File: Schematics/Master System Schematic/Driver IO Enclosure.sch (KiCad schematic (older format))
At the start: 5 parts, among them U11 CAN_Bus_Module, U12 KY-019

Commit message: Added Master Schematic Wiring
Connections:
- new net: A1.~ (~~D9), U11.~ (Serial_Clock) (x6)
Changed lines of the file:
@@
 EESchema Schematic File Version 4
+LIBS:Master System Schematic-cache
 EELAYER 30 0
 EELAYER END

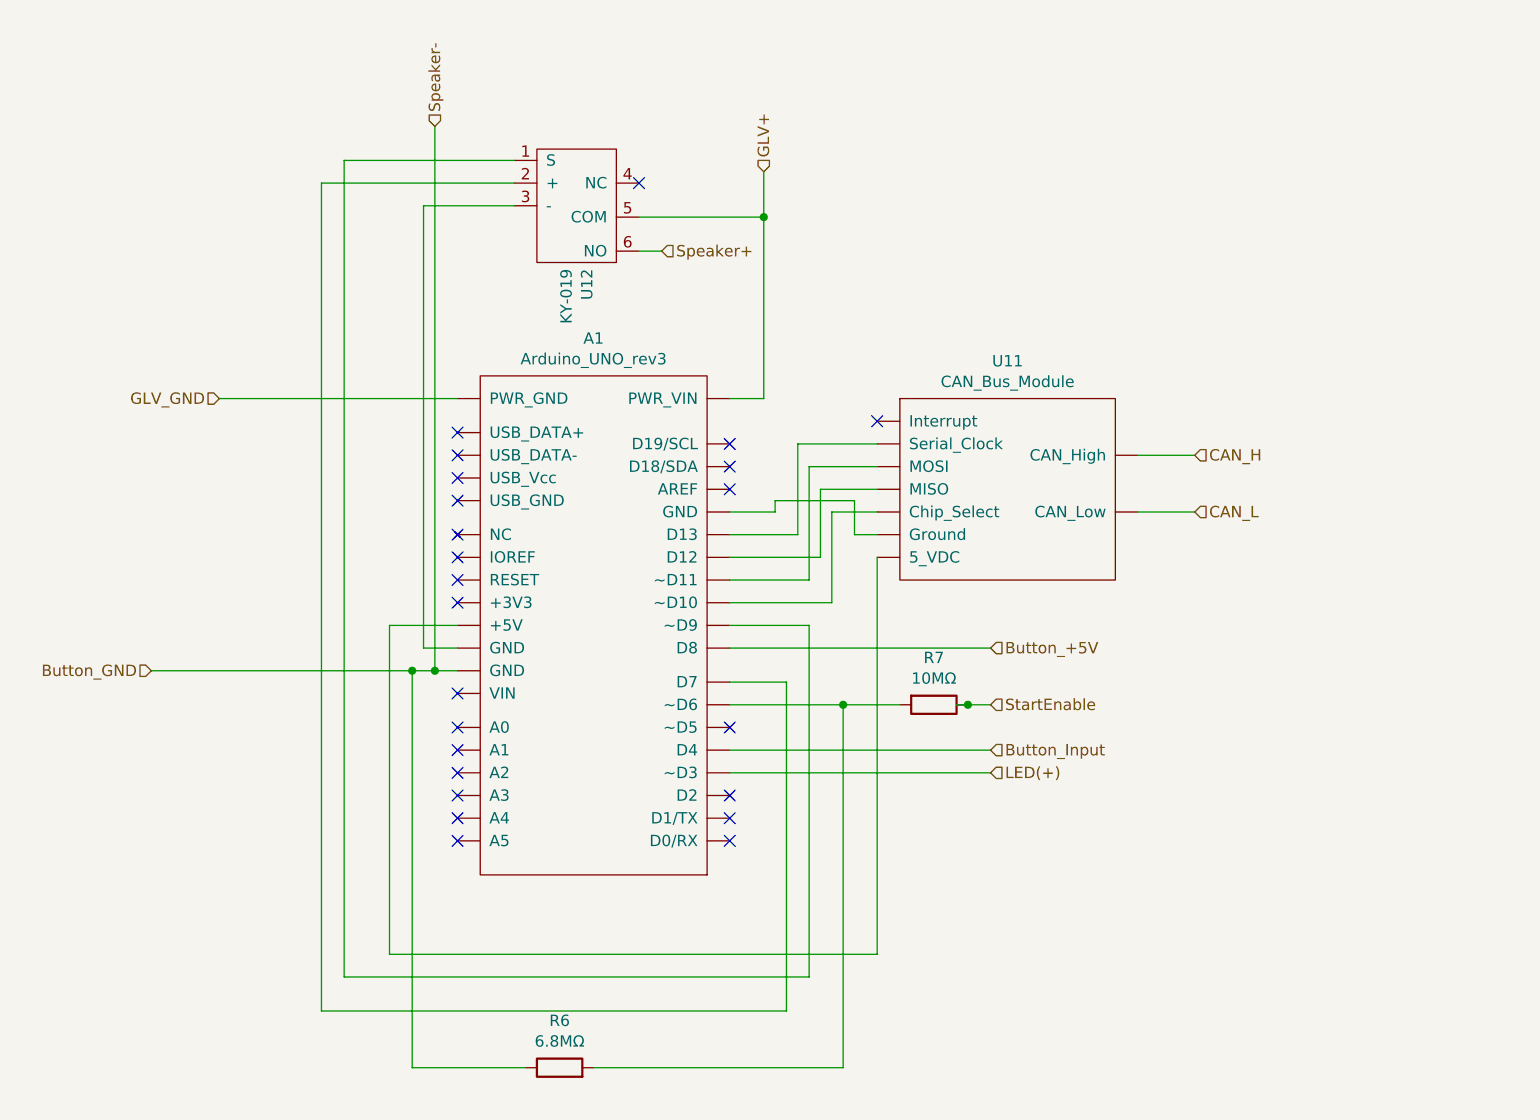
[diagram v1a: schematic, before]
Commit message: Cleaned up/Finalized Driver IO Schematic
Added a 100 ohm resistor to the 3v button to drop the 5v from the arduino to 3v. Cleaned up the messy wires.
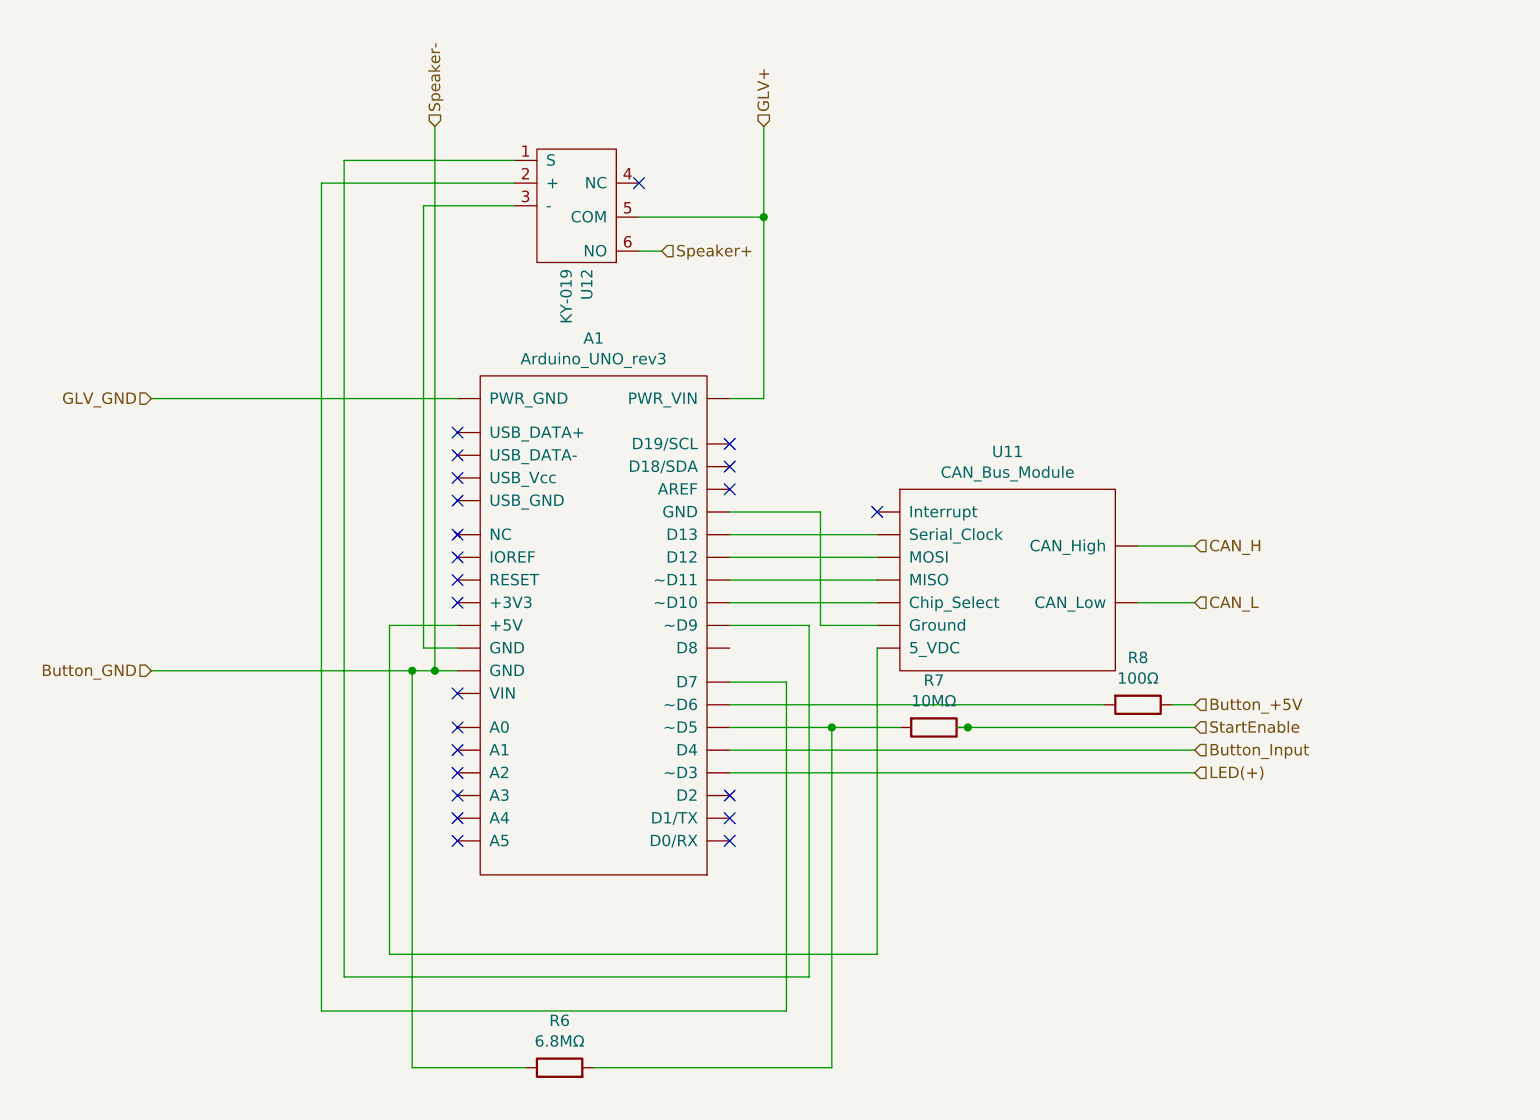
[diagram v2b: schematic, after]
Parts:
- added R8: 100Ω, symbol Device:R
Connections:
- net Button_+5V: now also R8.1; no longer A1.~ (~~D9)
- new net: A1.~ (~~D9), U11.~ (Serial_Clock) (x6)
- new net: A1.~ (~~D9), R8.2
- no-connect marks 24 -> 23
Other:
- moved on the sheet: R7, U11
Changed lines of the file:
@@
 EESchema Schematic File Version 4
-LIBS:Master System Schematic-cache
 EELAYER 30 0
 EELAYER END
@@
 $EndDescr
 $Comp
-L NER:CAN_Bus_Module U11
-U 1 1 5F847676
-P 7250 2900
-F 0 "U11" H 7275 3015 50  0000 C CNN
-F 1 "CAN_Bus_Module" H 7275 2924 50  0000 C CNN
-F 2 "" H 7250 2900 50  0001 C CNN
-F 3 "" H 7250 2900 50  0001 C CNN
-	1    7250 2900
-	1    0    0    -1
-$EndComp
-$Comp
 L NER:Arduino_UNO_rev3 A1
 U 1 1 5F848DBE
@@
 	0    1    1    0
 $EndComp
-Text HLabel 8100 3450 2    50   Input ~ 0
-CAN_L
-Wire Wire Line
-	8100 3450 7850 3450
-Text HLabel 8100 3200 2    50   Input ~ 0
-CAN_H
-Wire Wire Line
-	8100 3200 7850 3200
-Text HLabel 6200 1950 1    50   Input ~ 0
+Text HLabel 6200 1750 1    50   Input ~ 0
 GLV+
 Wire Wire Line
 	6200 2950 6050 2950
-NoConn ~ 6700 3050
-Wire Wire Line
-	6700 3150 6350 3150
-Wire Wire Line
-	6350 3150 6350 3550
-Wire Wire Line
-	6350 3550 6050 3550
-Wire Wire Line
-	6200 1950 6200 2150
 Wire Wire Line
 	6200 2150 5650 2150
@@
 	4750 1750 4750 4150
 Wire Wire Line
-	6700 3250 6400 3250
-Wire Wire Line
-	6400 3250 6400 3750
-Wire Wire Line
-	6400 3750 6050 3750
-Wire Wire Line
-	6700 3350 6450 3350
-Wire Wire Line
-	6450 3350 6450 3650
-Wire Wire Line
-	6450 3650 6050 3650
-Wire Wire Line
-	6700 3450 6500 3450
-Wire Wire Line
-	6500 3450 6500 3850
-Wire Wire Line
-	6500 3850 6050 3850
-Wire Wire Line
-	6700 3550 6600 3550
-Wire Wire Line
-	6600 3550 6600 3400
-Wire Wire Line
-	6600 3400 6250 3400
-Wire Wire Line
-	6250 3400 6250 3450
-Wire Wire Line
-	6250 3450 6050 3450
-Wire Wire Line
-	6700 3650 6700 5400
-Wire Wire Line
 	6700 5400 4550 5400
 Wire Wire Line
@@
 Wire Wire Line
 	6400 3950 6050 3950
-Text HLabel 3800 2950 0    50   Input ~ 0
+Text HLabel 3500 2950 0    50   Input ~ 0
 GLV_GND
-Wire Wire Line
-	4850 2950 3800 2950
 NoConn ~ 5650 2000
 Wire Wire Line
@@
 NoConn ~ 4850 4800
 NoConn ~ 4850 4900
-NoConn ~ 6050 4400
 NoConn ~ 6050 4700
 NoConn ~ 6050 4800
@@
 NoConn ~ 6050 3250
 NoConn ~ 6050 3350
-Wire Wire Line
-	6050 4600 7200 4600
-Text HLabel 7200 4600 2    50   Input ~ 0
+Text HLabel 8100 4600 2    50   Input ~ 0
 LED(+)
 Wire Wire Line
@@
 Text HLabel 3500 4150 0    50   Input ~ 0
 Button_GND
-Text HLabel 7200 4500 2    50   Input ~ 0
+Text HLabel 8100 4500 2    50   Input ~ 0
 Button_Input
-Wire Wire Line
-	6050 4500 7200 4500
-Text HLabel 7200 4050 2    50   Input ~ 0
+Text HLabel 8100 4300 2    50   Input ~ 0
 Button_+5V
-Wire Wire Line
-	6050 4050 7200 4050
 Text HLabel 5750 2300 2    50   Input ~ 0
 Speaker+
@@
 Wire Wire Line
 	5650 2300 5750 2300
-Text HLabel 7200 4300 2    50   Input ~ 0
-StartEnable
-$Comp
-L Device:R R7
-U 1 1 5F8BB898
-P 6950 4300
-F 0 "R7" V 6743 4300 50  0000 C CNN
-F 1 "10MΩ" V 6834 4300 50  0000 C CNN
-F 2 "" V 6880 4300 50  0001 C CNN
-F 3 "~" H 6950 4300 50  0001 C CNN
-	1    6950 4300
-	0    1    1    0
-$EndComp
-Wire Wire Line
-	7200 4300 7100 4300
-Connection ~ 7100 4300
-Wire Wire Line
-	7100 4300 7050 4300
-Wire Wire Line
-	6050 4300 6550 4300
 $Comp
 L Device:R R6
@@
 $EndComp
 Wire Wire Line
-	6550 4300 6550 5900
-Wire Wire Line
-	6550 5900 5450 5900
-Connection ~ 6550 4300
-Wire Wire Line
-	6550 4300 6800 4300
-Wire Wire Line
 	4650 5900 4650 4150
 Wire Wire Line
@@
 Wire Wire Line
 	4650 4150 4750 4150
+$Comp
+L Device:R R8
+U 1 1 5F8E0B40
+P 7850 4300
+F 0 "R8" V 7643 4300 50  0000 C CNN
+F 1 "100Ω" V 7734 4300 50  0000 C CNN
+F 2 "" V 7780 4300 50  0001 C CNN
+F 3 "~" H 7850 4300 50  0001 C CNN
+	1    7850 4300
+	0    1    1    0
+$EndComp
+Wire Wire Line
+	8000 4300 8100 4300
+NoConn ~ 6700 3450
+Wire Wire Line
+	8100 3600 7850 3600
+Text HLabel 8100 3600 2    50   Input ~ 0
+CAN_H
+Wire Wire Line
+	8100 3850 7850 3850
+Text HLabel 8100 3850 2    50   Input ~ 0
+CAN_L
+$Comp
+L NER:CAN_Bus_Module U11
+U 1 1 5F847676
+P 7250 3300
+F 0 "U11" H 7275 3415 50  0000 C CNN
+F 1 "CAN_Bus_Module" H 7275 3324 50  0000 C CNN
+F 2 "" H 7250 3300 50  0001 C CNN
+F 3 "" H 7250 3300 50  0001 C CNN
+	1    7250 3300
+	1    0    0    -1
+$EndComp
+Wire Wire Line
+	7100 4400 7050 4400
+Connection ~ 7100 4400
+$Comp
+L Device:R R7
+U 1 1 5F8BB898
+P 6950 4400
+F 0 "R7" V 6743 4400 50  0000 C CNN
+F 1 "10MΩ" V 6834 4400 50  0000 C CNN
+F 2 "" V 6880 4400 50  0001 C CNN
+F 3 "~" H 6950 4400 50  0001 C CNN
+	1    6950 4400
+	0    1    1    0
+$EndComp
+Text HLabel 8100 4400 2    50   Input ~ 0
+StartEnable
+Wire Wire Line
+	6050 4400 6500 4400
+Wire Wire Line
+	6500 4400 6500 5900
+Wire Wire Line
+	6500 5900 5450 5900
+Connection ~ 6500 4400
+Wire Wire Line
+	6500 4400 6800 4400
+Wire Wire Line
+	6050 3850 6700 3850
+Wire Wire Line
+	6050 3750 6700 3750
+Wire Wire Line
+	6050 3650 6700 3650
+Wire Wire Line
+	6050 3550 6700 3550
+Wire Wire Line
+	6700 3950 6450 3950
+Wire Wire Line
+	6450 3950 6450 3450
+Wire Wire Line
+	6450 3450 6050 3450
+Wire Wire Line
+	7100 4400 8100 4400
+Wire Wire Line
+	6050 4500 8100 4500
+Wire Wire Line
+	6050 4600 8100 4600
+Wire Wire Line
+	6700 4050 6700 5400
+Wire Wire Line
+	7700 4300 6050 4300
+Wire Wire Line
+	6200 1750 6200 2150
+Wire Wire Line
+	3500 2950 4850 2950
 $EndSCHEMATC

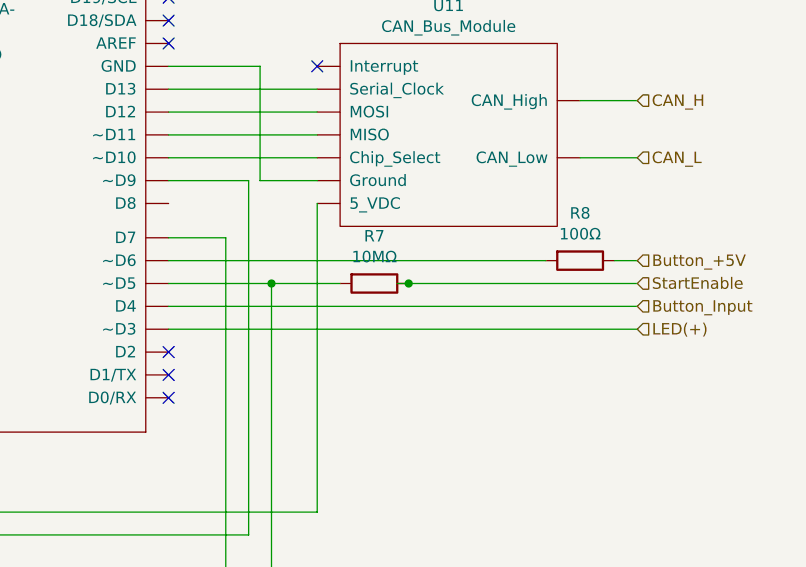
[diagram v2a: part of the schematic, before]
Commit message: Fixed an overlapping wire
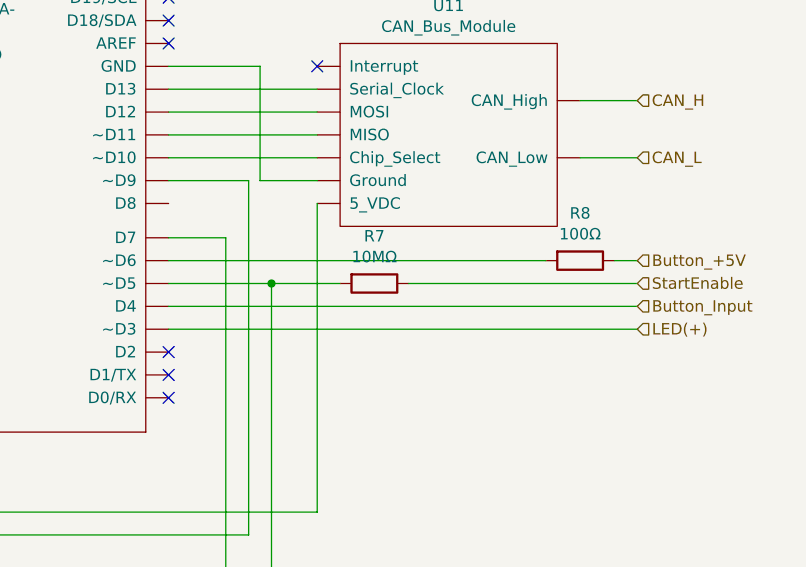
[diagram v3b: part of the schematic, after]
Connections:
- new net: A1.~ (~~D9), U11.~ (Serial_Clock) (x6)
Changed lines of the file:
@@
 EESchema Schematic File Version 4
+LIBS:Master System Schematic-cache
 EELAYER 30 0
 EELAYER END
@@
 	1    0    0    -1
 $EndComp
-Wire Wire Line
-	7100 4400 7050 4400
-Connection ~ 7100 4400
 $Comp
 L Device:R R7
